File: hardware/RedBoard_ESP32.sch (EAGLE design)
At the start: 109 parts, among them J1 5.5x2.1mm Barrel, J13 QWIIC_RIGHT_ANGLE, J15 MICRO-SDPUSH-PUSH, J2 USB C, J3 USB_SOLDER_PADS, J5 M10NO_SILK, Q1 MBT3904DW1T1, Q11 20V/4.2A/52mΩ/1.4W, Q13 20V/4.2A/52mΩ/1.4W, Q3 20V/4.2A/52mΩ/1.4W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

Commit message: Added missing Vin symbol.
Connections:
- removed net N$9: C9.+, D1.C, U3.IN
- net VIN: now also C9.+, D1.C, U3.IN
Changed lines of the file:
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@@
 <part name="LOGO3" library="SparkFun-Aesthetics" deviceset="OSHW-LOGO" device="MINI"/>
 <part name="LOGO4" library="SparkFun-Aesthetics" deviceset="QWIIC_LOGO" device="_5MM"/>
+<part name="SUPPLY28" library="SparkFun-PowerSymbols" deviceset="VIN" device=""/>
 </parts>
 <sheets>
@@
 <instance part="LOGO3" gate="G$1" x="317.5" y="12.7" smashed="yes"/>
 <instance part="LOGO4" gate="G$1" x="317.5" y="27.94" smashed="yes"/>
+<instance part="SUPPLY28" gate="G$1" x="142.24" y="129.54" smashed="yes">
+<attribute name="VALUE" x="142.24" y="132.334" size="1.778" layer="96" align="bottom-center"/>
+</instance>
 </instances>
 <busses>
@@
 <pinref part="SUPPLY13" gate="G$1" pin="VIN"/>
 </segment>
+<segment>
+<wire x1="144.78" y1="127" x2="142.24" y2="127" width="0.1524" layer="91"/>
+<wire x1="142.24" y1="124.46" x2="142.24" y2="127" width="0.1524" layer="91"/>
+<junction x="142.24" y="127"/>
+<pinref part="C9" gate="G$1" pin="+"/>
+<wire x1="142.24" y1="127" x2="134.62" y2="127" width="0.1524" layer="91"/>
+<pinref part="D1" gate="G$1" pin="C"/>
+<pinref part="U3" gate="G$1" pin="IN"/>
+<wire x1="142.24" y1="127" x2="142.24" y2="129.54" width="0.1524" layer="91" style="longdash"/>
+<pinref part="SUPPLY28" gate="G$1" pin="VIN"/>
+</segment>
 </net>
 <net name="VUSB" class="1">
@@
 </segment>
 </net>
-<net name="N$9" class="1">
-<segment>
-<wire x1="144.78" y1="127" x2="142.24" y2="127" width="0.1524" layer="91"/>
-<wire x1="142.24" y1="124.46" x2="142.24" y2="127" width="0.1524" layer="91"/>
-<junction x="142.24" y="127"/>
-<pinref part="C9" gate="G$1" pin="+"/>
-<wire x1="142.24" y1="127" x2="134.62" y2="127" width="0.1524" layer="91"/>
-<pinref part="D1" gate="G$1" pin="C"/>
-<pinref part="U3" gate="G$1" pin="IN"/>
-</segment>
-</net>

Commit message: Changed pin name from /SS to /CS
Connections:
- net ESP32_GPIO5_!SS! renamed ESP32_GPIO5_!CS!
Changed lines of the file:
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@@
 </segment>
 </net>
-<net name="ESP32_GPIO5_!SS!" class="0">
+<net name="ESP32_GPIO5_!CS!" class="0">
 <segment>
 <pinref part="U1" gate="U1" pin="CS3/IO5"/>

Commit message: Preliminary routed board, no labels yet.
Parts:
- LOGO1: value SFE_LOGO_NAME_FLAME6_MM -> SFE_LOGO_NAME.1_INCH; device SparkFun-Aesthetics:SFE_LOGO_NAME_FLAME6_MM -> SparkFun-Aesthetics:SFE_LOGO_NAME.1_INCH
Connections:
- removed net SHLD: J2.SHLD
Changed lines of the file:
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@@
 <setting verticaltext="up"/>
 </settings>
-<grid distance="0.1" unitdist="inch" unit="inch" style="lines" multiple="1" display="yes" altdistance="0.01" altunitdist="inch" altunit="inch"/>
+<grid distance="0.1" unitdist="inch" unit="inch" style="lines" multiple="1" display="no" altdistance="0.01" altunitdist="inch" altunit="inch"/>
 <layers>
 <layer number="1" name="Top" color="4" fill="1" visible="no" active="no"/>
@@
 <part name="D5" library="SparkFun-LED" deviceset="LED-GREEN" device="_HIDDENSILK" value="PWR"/>
 <part name="GND51" library="SparkFun-PowerSymbols" deviceset="GND" device=""/>
-<part name="LOGO1" library="SparkFun-Aesthetics" deviceset="SFE_LOGO_NAME_FLAME" device="6_MM"/>
+<part name="LOGO1" library="SparkFun-Aesthetics" deviceset="SFE_LOGO_NAME" device=".1_INCH" value="SFE_LOGO_NAME.1_INCH"/>
 <part name="LOGO2" library="SparkFun-Aesthetics" deviceset="QWIIC_LOGO" device="_5MM"/>
 <part name="LOGO3" library="SparkFun-Aesthetics" deviceset="OSHW-LOGO" device="MINI"/>
@@
 </segment>
 </net>
-<net name="SHLD" class="0">
-<segment>
-<wire x1="231.14" y1="223.52" x2="236.22" y2="223.52" width="0.1524" layer="91"/>
-<label x="236.22" y="223.52" size="1.27" layer="95" xref="yes"/>
-<pinref part="J2" gate="J1" pin="SHLD"/>
-</segment>
-</net>

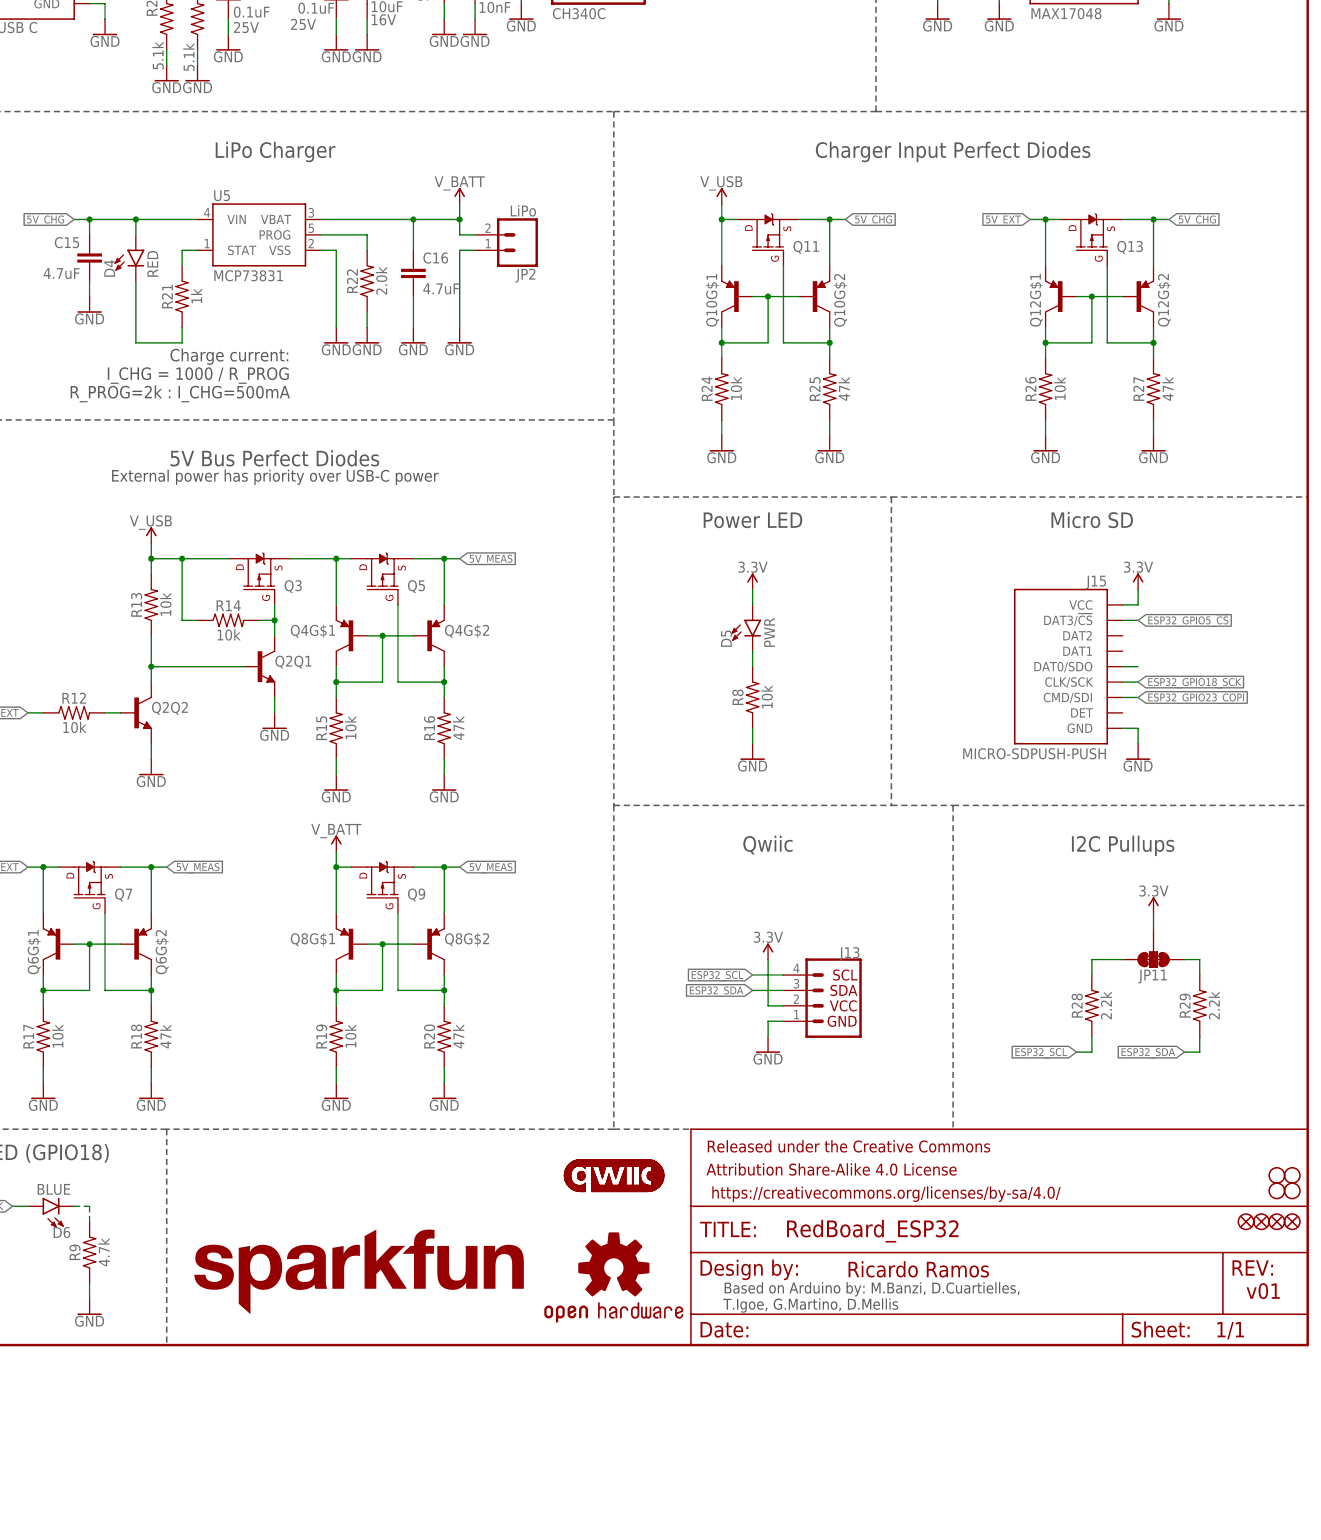
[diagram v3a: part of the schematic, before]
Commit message: Added board labels.
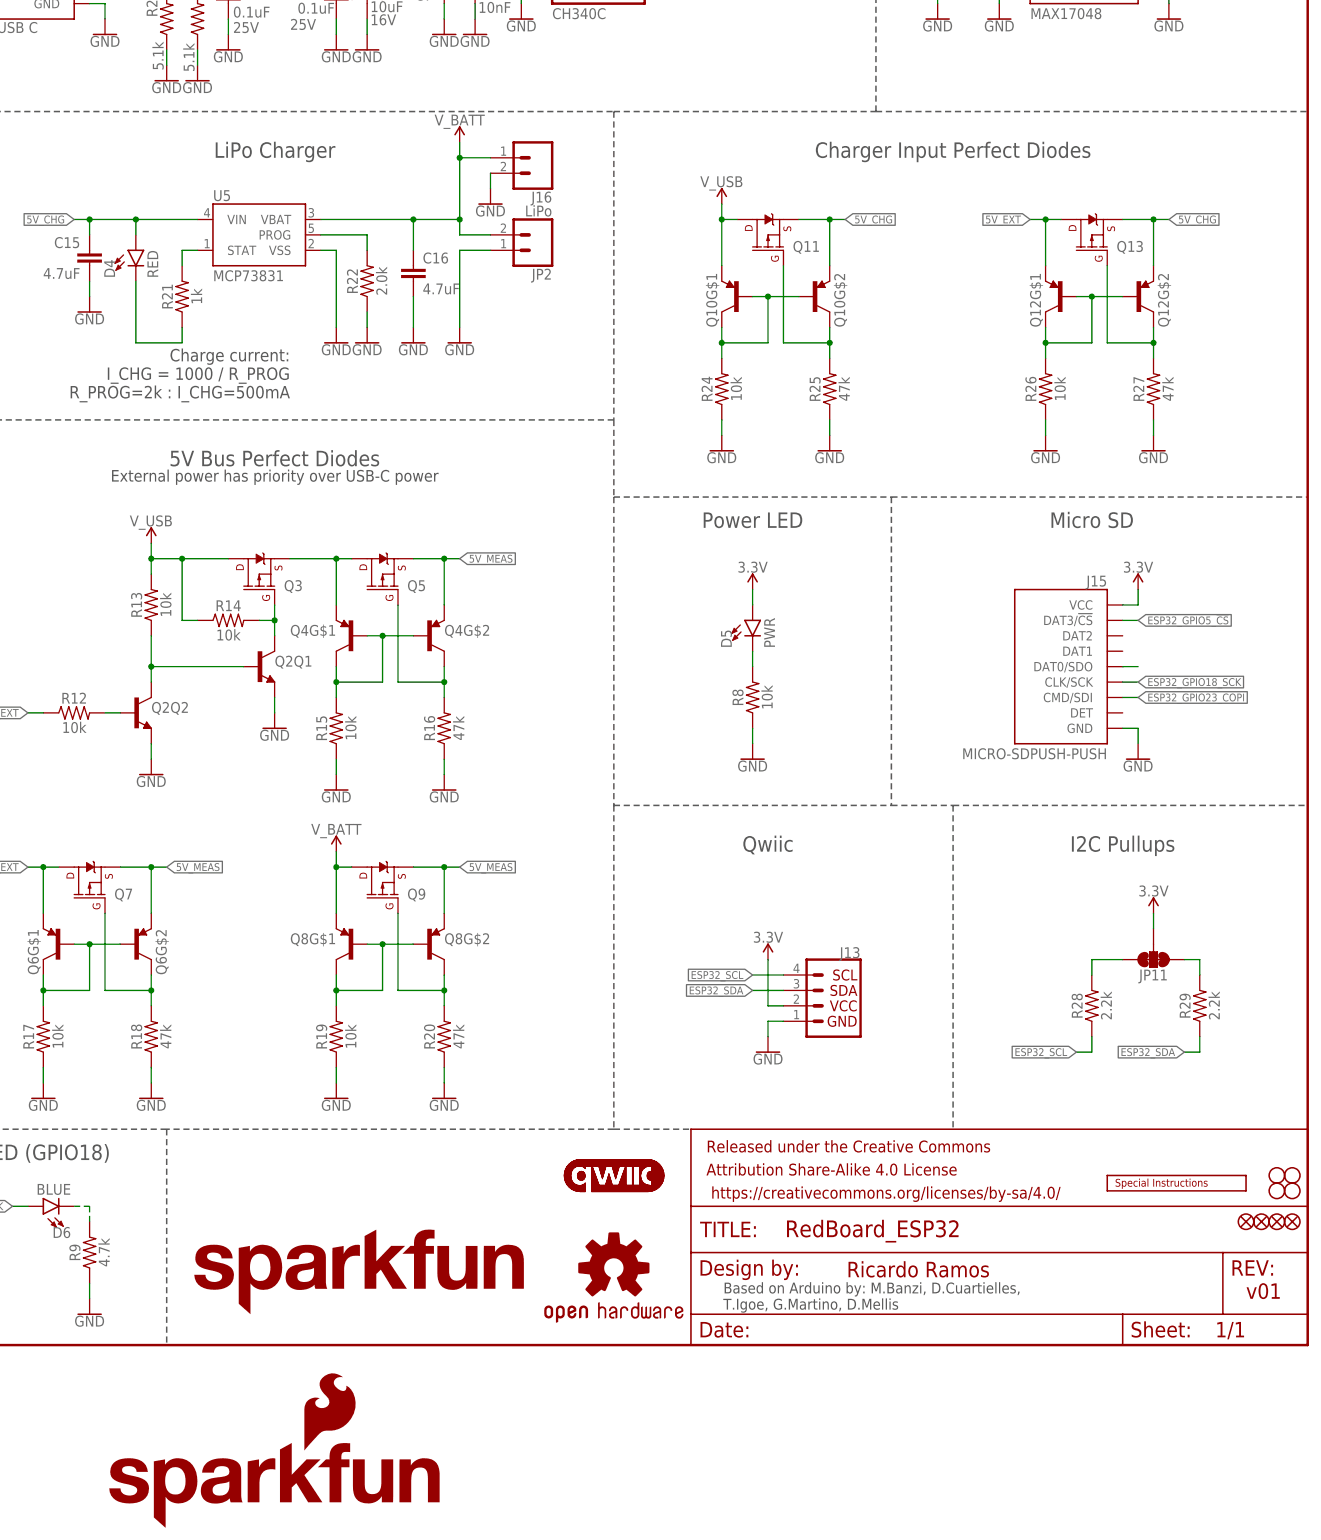
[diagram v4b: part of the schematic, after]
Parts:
- added J16: (no value), SparkFun-Connectors:CONN_02
- added LOGO5: SPECIAL_INSTRUCTIONS-ORDERING, SparkFun-Aesthetics:SPECIAL_INSTRUCTIONS-ORDERING
- added LOGO6: SFE_LOGO_NAME_FLAME.2_INCH, SparkFun-Aesthetics:SFE_LOGO_NAME_FLAME.2_INCH
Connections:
- net GND: now also J16.2
- net V_BATT: now also J16.1
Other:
- moved on the sheet: JP2
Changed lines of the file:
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@@
 <part name="LOGO4" library="SparkFun-Aesthetics" deviceset="QWIIC_LOGO" device="_5MM"/>
 <part name="SUPPLY28" library="SparkFun-PowerSymbols" deviceset="VIN" device=""/>
+<part name="LOGO5" library="SparkFun-Aesthetics" deviceset="SPECIAL_INSTRUCTIONS" device="-ORDERING"/>
+<part name="J16" library="SparkFun-Connectors" deviceset="CONN_02" device=""/>
+<part name="GND53" library="SparkFun-PowerSymbols" deviceset="GND" device=""/>
+<part name="LOGO6" library="SparkFun-Aesthetics" deviceset="SFE_LOGO_NAME_FLAME" device=".2_INCH" value="SFE_LOGO_NAME_FLAME.2_INCH"/>
 </parts>
 <sheets>
@@
 <attribute name="VALUE" x="286.004" y="173.101" size="1.778" layer="96" font="vector"/>
 </instance>
-<instance part="JP2" gate="G$1" x="302.26" y="182.88" smashed="yes" rot="R180">
-<attribute name="VALUE" x="304.8" y="187.706" size="1.778" layer="96" font="vector" rot="R180"/>
-<attribute name="NAME" x="304.8" y="177.292" size="1.778" layer="95" font="vector" rot="R180"/>
+<instance part="JP2" gate="G$1" x="304.8" y="182.88" smashed="yes" rot="R180">
+<attribute name="VALUE" x="307.34" y="187.706" size="1.778" layer="96" font="vector" rot="R180"/>
+<attribute name="NAME" x="307.34" y="177.292" size="1.778" layer="95" font="vector" rot="R180"/>
 </instance>
 <instance part="R21" gate="G$1" x="246.38" y="172.72" smashed="yes" rot="R90">
@@
 <attribute name="VALUE" x="240.665" y="175.768" size="1.778" layer="96" font="vector" rot="R90" align="top-left"/>
 </instance>
-<instance part="SUPPLY4" gate="G$1" x="292.1" y="187.96" smashed="yes">
-<attribute name="VALUE" x="292.1" y="190.754" size="1.778" layer="96" align="bottom-center"/>
+<instance part="SUPPLY4" gate="G$1" x="292.1" y="198.12" smashed="yes">
+<attribute name="VALUE" x="292.1" y="200.914" size="1.778" layer="96" align="bottom-center"/>
 </instance>
 <instance part="GND4" gate="1" x="231.14" y="170.18" smashed="yes">
@@
 <attribute name="VALUE" x="142.24" y="132.334" size="1.778" layer="96" align="bottom-center"/>
 </instance>
+<instance part="LOGO5" gate="G$1" x="398.78" y="25.4" smashed="yes"/>
+<instance part="J16" gate="G$1" x="304.8" y="195.58" smashed="yes" rot="R180">
+<attribute name="VALUE" x="307.34" y="200.406" size="1.778" layer="96" font="vector" rot="R180"/>
+<attribute name="NAME" x="307.34" y="189.992" size="1.778" layer="95" font="vector" rot="R180"/>
+</instance>
+<instance part="GND53" gate="1" x="297.18" y="187.96" smashed="yes">
+<attribute name="VALUE" x="297.18" y="187.706" size="1.778" layer="96" align="top-center"/>
+</instance>
+<instance part="LOGO6" gate="G$1" x="233.68" y="-30.48" smashed="yes"/>
 </instances>
 <busses>
@@
 <segment>
 <wire x1="292.1" y1="180.34" x2="292.1" y2="167.64" width="0.1524" layer="91"/>
-<wire x1="292.1" y1="180.34" x2="294.64" y2="180.34" width="0.1524" layer="91"/>
+<wire x1="292.1" y1="180.34" x2="297.18" y2="180.34" width="0.1524" layer="91"/>
 <pinref part="JP2" gate="G$1" pin="2"/>
 <pinref part="GND31" gate="1" pin="GND"/>
@@
 <wire x1="340.36" y1="101.6" x2="340.36" y2="99.06" width="0.1524" layer="91"/>
 <pinref part="GND51" gate="1" pin="GND"/>
+</segment>
+<segment>
+<pinref part="J16" gate="G$1" pin="2"/>
+<wire x1="297.18" y1="193.04" x2="297.18" y2="190.5" width="0.1524" layer="91"/>
+<pinref part="GND53" gate="1" pin="GND"/>
 </segment>
 </net>
@@
 <segment>
 <wire x1="292.1" y1="182.88" x2="292.1" y2="185.42" width="0.1524" layer="91"/>
-<wire x1="292.1" y1="185.42" x2="292.1" y2="187.96" width="0.1524" layer="91"/>
+<wire x1="292.1" y1="185.42" x2="292.1" y2="195.58" width="0.1524" layer="91"/>
+<wire x1="292.1" y1="195.58" x2="292.1" y2="198.12" width="0.1524" layer="91"/>
 <wire x1="284.48" y1="180.34" x2="284.48" y2="185.42" width="0.1524" layer="91"/>
 <wire x1="292.1" y1="185.42" x2="284.48" y2="185.42" width="0.1524" layer="91"/>
@@
 <junction x="284.48" y="185.42"/>
 <wire x1="284.48" y1="185.42" x2="269.24" y2="185.42" width="0.1524" layer="91"/>
-<wire x1="292.1" y1="182.88" x2="294.64" y2="182.88" width="0.1524" layer="91"/>
+<wire x1="292.1" y1="182.88" x2="297.18" y2="182.88" width="0.1524" layer="91"/>
 <pinref part="U5" gate="G$1" pin="VBAT"/>
 <pinref part="C16" gate="G$1" pin="1"/>
 <pinref part="JP2" gate="G$1" pin="1"/>
 <pinref part="SUPPLY4" gate="G$1" pin="V_BATT"/>
-</segment>
-<segment>
+<pinref part="J16" gate="G$1" pin="1"/>
+<wire x1="297.18" y1="195.58" x2="292.1" y2="195.58" width="0.1524" layer="91"/>
+<junction x="292.1" y="195.58"/>
+</segment>
+<segment>

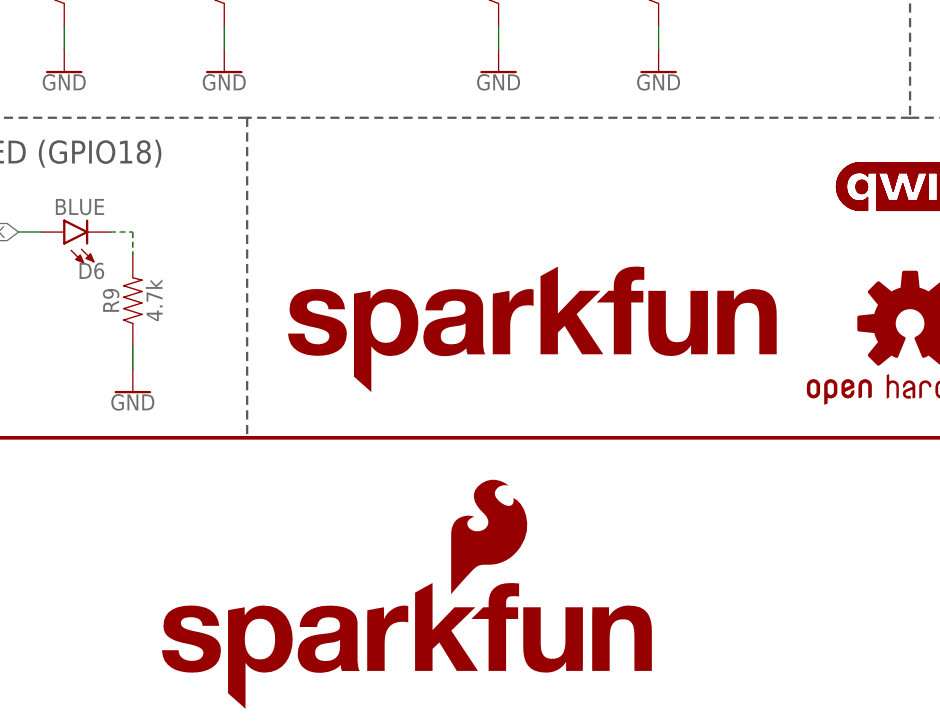
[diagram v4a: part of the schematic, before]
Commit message: Added ordering instructions; added production files.
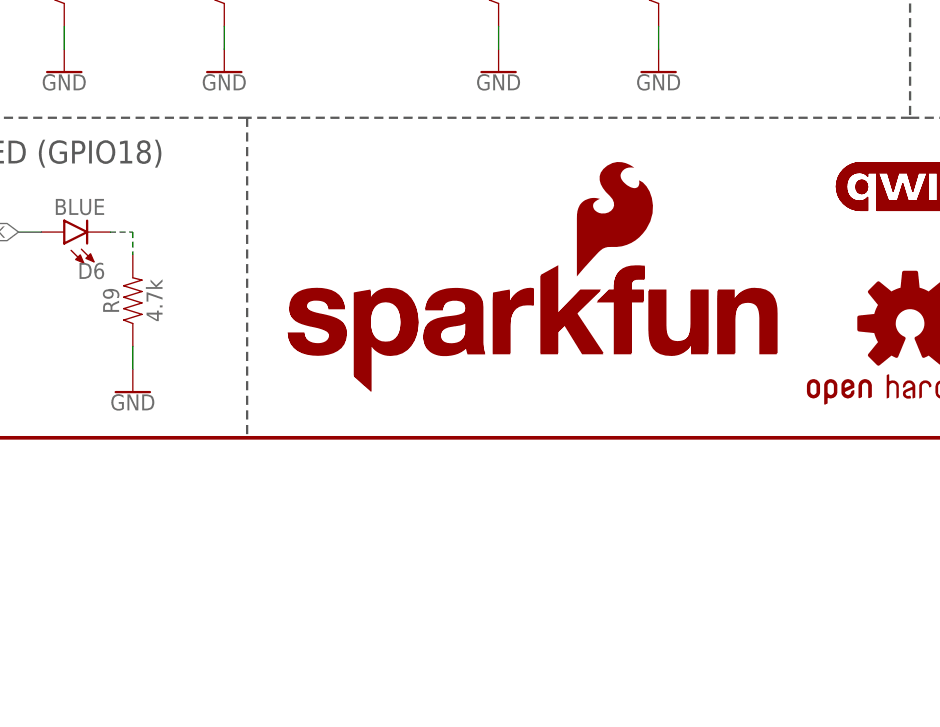
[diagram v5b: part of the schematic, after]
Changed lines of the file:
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@@
 <attribute name="VALUE" x="297.18" y="187.706" size="1.778" layer="96" align="top-center"/>
 </instance>
-<instance part="LOGO6" gate="G$1" x="233.68" y="-30.48" smashed="yes"/>
+<instance part="LOGO6" gate="G$1" x="247.65" y="4.826" smashed="yes"/>
 </instances>
 <busses>
